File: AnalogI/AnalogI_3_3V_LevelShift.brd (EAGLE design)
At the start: 64 x 82 mm, 80 parts, among them IC1 HCPL-7800, IC2 HCPL-7800, IC3 HCPL-7800, IC4 HCPL-7800, IC5 MCP3424SOIC, IC6 74HC4051_MUXN, IC7 74HC4051_MUXN, P1 DF11-06-2DSA, Q1 BS170, Q2 BS170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

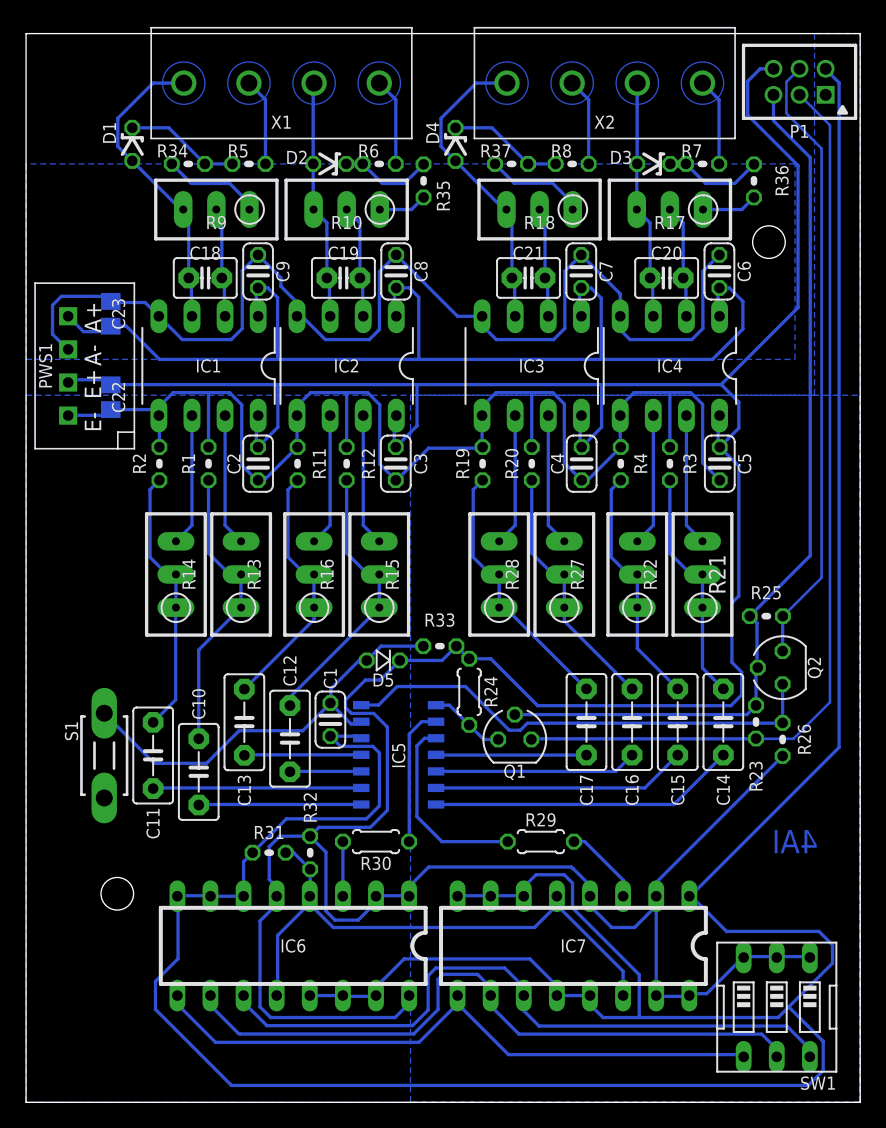
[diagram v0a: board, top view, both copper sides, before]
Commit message: Change connector. Modified solder mask.
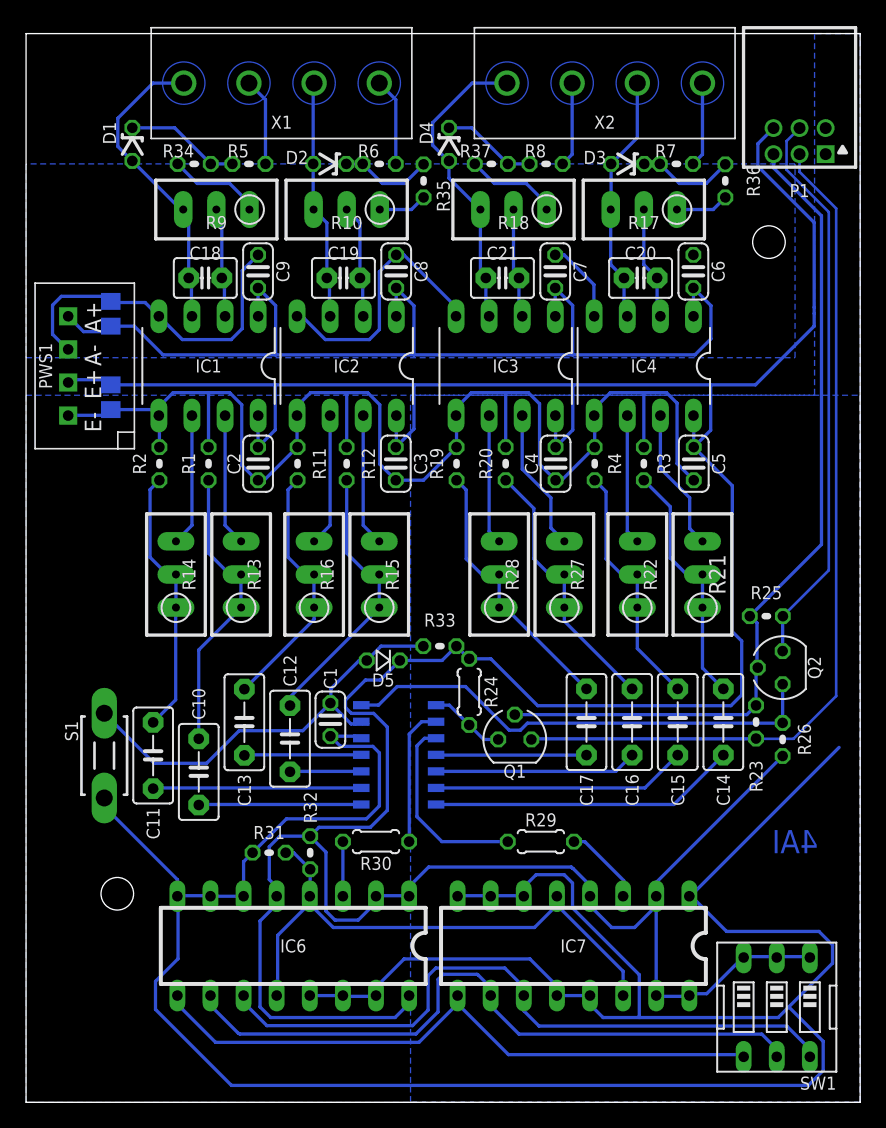
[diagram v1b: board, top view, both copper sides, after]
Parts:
- P1: value DF11-06-2DSA -> DF11-06-2DS; device con-hirose-df11:DF11-06DP-2DSA -> con-hirose-df11:DF11-06DP-2DS
- moved P1 4.55 mm to (59.4, 73.8)
- moved R36 2.20 mm to (53.6, 70.7)
- moved C20 2.00 mm to (47.1, 63.2)
- moved C21 2.00 mm to (36.5, 63.2)
- moved C4 2.00 mm to (40.6, 49.0)
- moved C5 2.00 mm to (51.2, 49.0)
- moved C6 2.00 mm to (51.2, 63.8)
- moved C7 2.00 mm to (40.6, 63.8)
- moved D3 2.00 mm to (46.2, 72.0)
- moved IC3 2.00 mm to (36.8, 56.5)
- moved IC4 2.00 mm to (47.4, 56.5)
- moved R17 2.00 mm to (47.4, 68.5)
- moved R18 2.00 mm to (37.4, 68.5)
- moved R19 2.00 mm to (33.0, 49.0)
- moved R20 2.00 mm to (36.8, 49.0)
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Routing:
- net GND: track 361.6 -> 316.6 mm
- net N$33: track 89.1 -> 53.7 mm
- net N$8: track 88.0 -> 81.6 mm
- net +5V: track 288.0 -> 283.7 mm
- net N$71: track 71.8 -> 67.6 mm
- net N$69: track 47.6 -> 43.5 mm
- net +3V3: track 69.3 -> 65.3 mm
- net N$35: track 8.83 -> 7.33 mm
- net N$42: track 18.2 -> 19.2 mm
- net N$46: track 19.7 -> 20.7 mm
- net N$44: track 10.2 -> 11.0 mm
- net N$38: track 10.2 -> 11.0 mm
- net N$41: track 18.5 -> 19.3 mm
- net N$45: track 20.9 -> 21.5 mm
- net N$40: track 18.8 -> 19.4 mm

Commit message: Move DC/DC coppler. Update Gerbers.
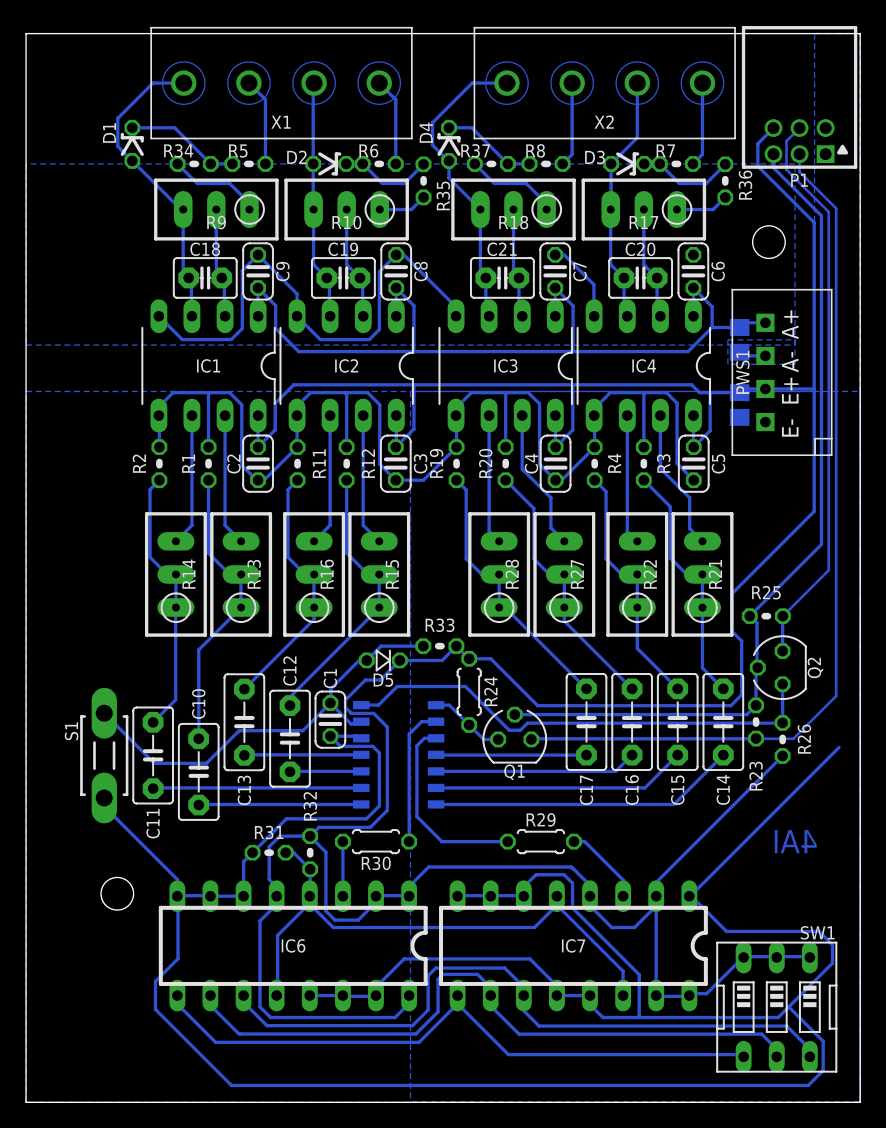
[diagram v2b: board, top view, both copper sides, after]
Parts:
- moved PWS1 53.5 mm to (58.0, 56.0)
- moved C23 48.3 mm to (54.8, 58.5), turned to 90 degrees
- moved C22 48.3 mm to (54.8, 53.5)
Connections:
- net N$33 renamed AGND
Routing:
- net N$8: track 81.6 -> 66.1 mm
- net +5V: track 283.7 -> 275.3 mm
- net GND: track 316.6 -> 309.3 mm
- net AGND: track 53.7 -> 48.7 mm

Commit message: Add load resistor.
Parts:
- added R38: 220, rcl:0204V
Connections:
- net AGND: now also R38.1
- net N$8: now also R38.2
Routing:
- net AGND: track 48.7 -> 93.8 mm
- net N$8: track 66.1 -> 79.3 mm
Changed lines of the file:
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@@
 <attribute name="NAME" x="53.2" y="53.5" size="1" layer="26" font="vector" ratio="10" rot="MR270" align="center"/>
+</element>
+<element name="R38" library="rcl" package="0204V" value="220" x="7" y="58.88" smashed="yes" rot="R270">
+<attribute name="NAME" x="7" y="61.35" size="1" layer="25" font="vector" ratio="10" rot="R270" align="center-right"/>
+<attribute name="VALUE" x="4.6886" y="61.0136" size="1.27" layer="27" ratio="10" rot="R270"/>
 </element>
 </elements>
@@
 <wire x1="28.41" y1="60.31" x2="28.4" y2="60.32" width="0.254" layer="16"/>
 <wire x1="28.4" y1="60.32" x2="28.4" y2="62.48" width="0.254" layer="16"/>
-<wire x1="17.8" y1="62.48" x2="19.15" y2="61.13" width="0.254" layer="16"/>
 <wire x1="17.81" y1="60.31" x2="17.8" y2="60.32" width="0.254" layer="16"/>
 <wire x1="17.8" y1="60.32" x2="17.8" y2="62.48" width="0.254" layer="16"/>
-<wire x1="19.15" y1="61.13" x2="19.15" y2="59.37" width="0.254" layer="16"/>
-<wire x1="19.15" y1="59.37" x2="20.92" y2="57.6" width="0.254" layer="16"/>
-<wire x1="20.92" y1="57.6" x2="29.76" y2="57.6" width="0.254" layer="16"/>
+<wire x1="19.15" y1="57.6" x2="29.76" y2="57.6" width="0.254" layer="16"/>
 <wire x1="29.76" y1="57.6" x2="41.97" y2="57.6" width="0.254" layer="16"/>
 <wire x1="41.97" y1="57.6" x2="50.79" y2="57.6" width="0.254" layer="16"/>
@@
 <wire x1="51.2" y1="62.48" x2="52.64" y2="61.04" width="0.254" layer="16"/>
 <wire x1="52.64" y1="61.04" x2="52.64" y2="59.45" width="0.254" layer="16"/>
+<contactref element="R38" pad="2"/>
+<wire x1="7" y1="57.61" x2="7.01" y2="57.6" width="0.254" layer="16"/>
+<wire x1="7.01" y1="57.6" x2="19.15" y2="57.6" width="0.254" layer="16"/>
+<wire x1="17.8" y1="62.48" x2="19.15" y2="61.13" width="0.254" layer="16"/>
+<wire x1="19.15" y1="61.13" x2="19.15" y2="57.6" width="0.254" layer="16"/>
 </signal>
 <signal name="N$41">
@@
 <contactref element="IC3" pad="4"/>
 <contactref element="C6" pad="2"/>
-<wire x1="10.16" y1="60.3504" x2="10.19" y2="60.31" width="0.254" layer="16"/>
 <wire x1="10.3632" y1="60.1472" x2="11.9888" y2="58.5216" width="0.254" layer="16"/>
 <wire x1="10.3632" y1="60.1472" x2="10.19" y2="60.31" width="0.254" layer="16"/>
 <wire x1="11.9888" y1="58.5216" x2="15.7416" y2="58.5216" width="0.254" layer="16"/>
 <wire x1="15.7416" y1="58.5216" x2="16.59" y2="59.37" width="0.254" layer="16"/>
-<wire x1="22.5784" y1="58.5216" x2="26.3416" y2="58.5216" width="0.254" layer="16"/>
-<wire x1="26.3416" y1="58.5216" x2="27.11" y2="59.29" width="0.254" layer="16"/>
 <polygon width="0.1524" layer="16" isolate="0.3048" thermals="no">
 <vertex x="0" y="58.1"/>
@@
 <wire x1="16.59" y1="59.37" x2="16.59" y2="63.81" width="0.254" layer="16"/>
 <wire x1="16.59" y1="63.81" x2="17.8" y2="65.02" width="0.254" layer="16"/>
-<wire x1="27.11" y1="59.29" x2="27.11" y2="63.73" width="0.254" layer="16"/>
-<wire x1="27.11" y1="63.73" x2="28.4" y2="65.02" width="0.254" layer="16"/>
 <wire x1="28.41" y1="65.03" x2="28.4" y2="65.02" width="0.254" layer="16"/>
 <contactref element="C23" pad="1"/>
@@
 <wire x1="43.57" y1="62.74" x2="43.57" y2="60.33" width="0.254" layer="16"/>
 <wire x1="43.57" y1="60.33" x2="43.59" y2="60.31" width="0.254" layer="16"/>
-<wire x1="20.79" y1="60.31" x2="22.5784" y2="58.5216" width="0.254" layer="16"/>
 <wire x1="20.79" y1="60.31" x2="20.79" y2="62.03" width="0.254" layer="16"/>
 <wire x1="20.79" y1="62.03" x2="17.8" y2="65.02" width="0.254" layer="16"/>
@@
 <wire x1="54.75" y1="57.55" x2="55.03" y2="57.27" width="0.254" layer="16"/>
 <wire x1="55.03" y1="57.27" x2="56.73" y2="57.27" width="0.254" layer="16"/>
+<contactref element="R38" pad="1"/>
+<wire x1="20.79" y1="60.31" x2="20.79" y2="59.94" width="0.254" layer="16"/>
+<wire x1="20.79" y1="59.94" x2="22.21" y2="58.52" width="0.254" layer="16"/>
+<wire x1="22.21" y1="58.52" x2="26.35" y2="58.52" width="0.254" layer="16"/>
+<wire x1="26.35" y1="58.52" x2="27.12" y2="59.29" width="0.254" layer="16"/>
+<wire x1="27.12" y1="59.29" x2="27.12" y2="63.74" width="0.254" layer="16"/>
+<wire x1="27.12" y1="63.74" x2="28.4" y2="65.02" width="0.254" layer="16"/>
+<wire x1="33.01" y1="60.33" x2="33.01" y2="59.67" width="0.254" layer="16"/>
+<wire x1="33.01" y1="59.67" x2="34.16" y2="58.52" width="0.254" layer="16"/>
+<wire x1="34.16" y1="58.52" x2="38.55" y2="58.52" width="0.254" layer="16"/>
+<wire x1="38.55" y1="58.52" x2="39.4" y2="59.37" width="0.254" layer="16"/>
+<wire x1="39.4" y1="59.37" x2="39.4" y2="63.82" width="0.254" layer="16"/>
+<wire x1="39.4" y1="63.82" x2="40.6" y2="65.02" width="0.254" layer="16"/>
+<wire x1="51.2" y1="65.02" x2="52.92" y2="65.02" width="0.254" layer="16"/>
+<wire x1="52.92" y1="65.02" x2="56.48" y2="61.46" width="0.254" layer="16"/>
+<wire x1="56.48" y1="61.46" x2="57.21" y2="61.46" width="0.254" layer="16"/>
+<wire x1="57.21" y1="61.46" x2="58.51" y2="60.16" width="0.254" layer="16"/>
+<wire x1="58.51" y1="60.16" x2="58.51" y2="57.87" width="0.254" layer="16"/>
+<wire x1="58.51" y1="57.87" x2="57.93" y2="57.29" width="0.254" layer="16"/>
+<wire x1="57.93" y1="57.29" x2="56.75" y2="57.29" width="0.254" layer="16"/>
+<wire x1="56.75" y1="57.29" x2="56.73" y2="57.27" width="0.254" layer="16"/>
+<wire x1="51.2" y1="65.02" x2="49.92" y2="63.74" width="0.254" layer="16"/>
+<wire x1="49.92" y1="63.74" x2="49.92" y2="59.45" width="0.254" layer="16"/>
+<wire x1="49.92" y1="59.45" x2="48.99" y2="58.52" width="0.254" layer="16"/>
+<wire x1="48.99" y1="58.52" x2="44.57" y2="58.52" width="0.254" layer="16"/>
+<wire x1="44.57" y1="58.52" x2="43.59" y2="59.5" width="0.254" layer="16"/>
+<wire x1="43.59" y1="59.5" x2="43.59" y2="60.31" width="0.254" layer="16"/>
+<wire x1="7" y1="60.15" x2="7.16" y2="60.31" width="0.254" layer="16"/>
+<wire x1="7.16" y1="60.31" x2="10.19" y2="60.31" width="0.254" layer="16"/>
 </signal>
 <signal name="N$49">
